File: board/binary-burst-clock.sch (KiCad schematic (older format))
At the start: 24 parts, among them J1 USB, P01 CONN_5, P02 CONN_5, P03 CONN_5, P04 CONN_5, P05 CONN_5, P06 CONN_5, P07 CONN_5, P08 CONN_5, P09 CONN_5, P10 CONN_5, P11 CONN_5, P12 CONN_5, Q1 2907A, Q2 2907A, Q3 2907A, Q4 2907A, U1 ATTINY44, U2 MCP7940N, U3 STP16CP05MTR

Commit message: More schematic work
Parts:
- added CONN1: K3000, symbol K3000
- added J2: AVR-ISP-6, AVR-ISP-6, symbol AVR-ISP-6
- added R?: R, symbol R
- added SW1, SW2: SW_PUSH, symbol SW_PUSH
- added X1: 32.768 kHz CRYSTAL, symbol CRYSTAL
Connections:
- net labels added: +BATT, PA5, Reset, SCL, SDA
- wire segments 102 -> 136
- no-connect marks 6 -> 7
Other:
- note added: "CR1220 Backup Battery"
- moved on the sheet: P01, P02, P03, P04, P05, P06, P07, P08, P09, P10, P11, P12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

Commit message: Full schematic finished
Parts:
- added R? (x4): 1k, symbol R
- added R? (x3): 2056, symbol R
- R?: value R -> 10k
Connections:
- net labels added: Blue0, Blue1, Blue2, Clock, Data, Latch, PA7, Red0
- wire segments 136 -> 169
- no-connect marks 7 -> 8
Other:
- moved on the sheet: P01, P02, P03, P04, P05, P06, P07, P12, R?, SW1, SW2, U1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

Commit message: All footprints created and assigned
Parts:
- removed J2: AVR-ISP-6, AVR-ISP-6, symbol AVR-ISP-6
- added CON1: AVR-ISP-6-FIXED, AVR_ISP_6-fixed, symbol AVR-ISP-6-FIXED
- P1: renamed from P01; value CONN_5 -> 1:00
- P10: value CONN_5 -> 10:00
- P11: value CONN_5 -> 11:00
- P12: value CONN_5 -> 12:00
- P2: renamed from P02; value CONN_5 -> 2:00
- P3: renamed from P03; value CONN_5 -> 3:00
- P4: renamed from P04; value CONN_5 -> 4:00
- P5: renamed from P05; value CONN_5 -> 5:00
- P6: renamed from P06; value CONN_5 -> 6:00
- P7: renamed from P07; value CONN_5 -> 7:00
- P8: renamed from P08; value CONN_5 -> 8:00
- P9: renamed from P09; value CONN_5 -> 9:00
- gave numbers to parts that had none: 8
- renumbered R3 to R4
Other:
- moved on the sheet: C3

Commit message: Finished first version of PCB
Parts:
- SW1: value SW_PUSH -> Hours
- SW2: value SW_PUSH -> Minutes
- X1: value 32.768 kHz CRYSTAL -> 32.768
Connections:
- wire segments 169 -> 167
- no-connect marks 8 -> 9

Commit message: Added I2C and power header; adjusted spacing
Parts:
- added P13: I2C, symbol CONN_4
- added P14: Power, symbol CONN_2
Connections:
- wire segments 167 -> 177

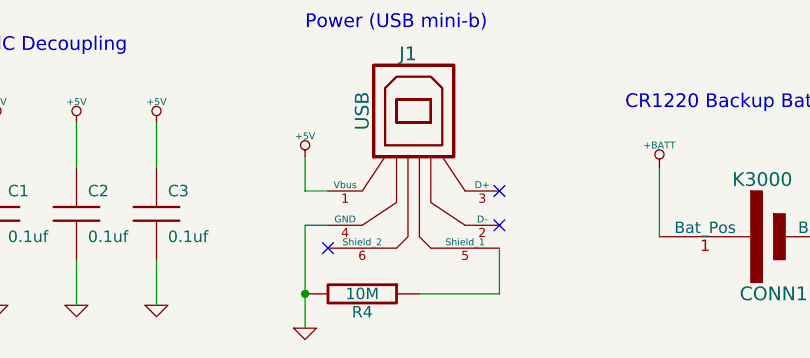
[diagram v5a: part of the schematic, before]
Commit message: Widened all traces (rerouting as neccessary) and removed 10M resistor from USB shielding pin.
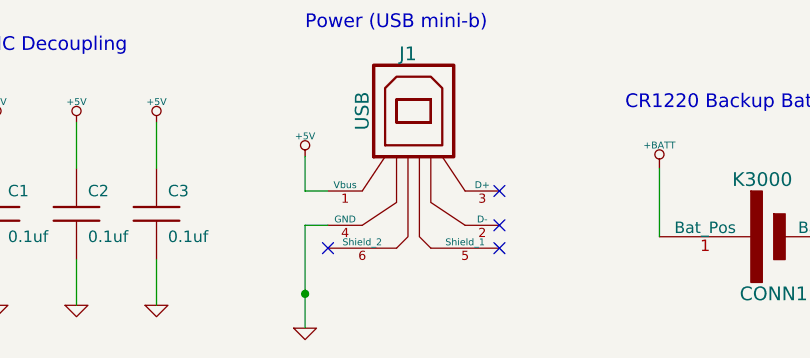
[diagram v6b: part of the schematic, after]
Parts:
- removed R4: 10M, symbol R
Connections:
- wire segments 177 -> 175
- no-connect marks 9 -> 10
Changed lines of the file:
@@
-EESchema Schematic File Version 2  date Mon 26 Dec 2011 10:55:31 AM CST
+EESchema Schematic File Version 2  date Sat 31 Dec 2011 04:27:24 PM CST
 LIBS:power
 LIBS:k3000
@@
 Sheet 1 1
 Title ""
-Date "26 dec 2011"
+Date "31 dec 2011"
 Rev ""
 Comp ""
@@
 Comment4 ""
 $EndDescr
+NoConn ~ 3400 7000
 Wire Wire Line
 	1100 5350 1100 5150
@@
 Wire Wire Line
 	5600 1700 5850 1700
-Wire Wire Line
-	3050 7200 3400 7200
-Wire Wire Line
-	3400 7200 3400 7000
 Wire Wire Line
 	6250 3950 5800 3950
@@
 $EndComp
 $Comp
-L R R4
-U 1 1 4EEDEFC3
-P 2800 7200
-F 0 "R4" V 2880 7200 50  0000 C CNN
-F 1 "10M" V 2800 7200 50  0000 C CNN
-	1    2800 7200
-	0    1    1    0
-$EndComp
-$Comp

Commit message: Fixed USB connector pinout; Adjusted solder stop of SOIC packages; moved labels on silk screen
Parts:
- removed J1: USB, symbol USB
- added J1: MINI_USB-B, symbol MINI_USB-B
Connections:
- no-connect marks 10 -> 9
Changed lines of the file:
@@
-EESchema Schematic File Version 2  date Sat 31 Dec 2011 04:27:24 PM CST
+EESchema Schematic File Version 2  date Sun 01 Jan 2012 04:04:24 PM CST
 LIBS:power
 LIBS:k3000
@@
 LIBS:valves
 LIBS:avr-isp-6
+LIBS:mini_usb-b
 LIBS:binary-burst-clock-cache
 EELAYER 25  0
@@
 Sheet 1 1
 Title ""
-Date "31 dec 2011"
+Date "1 jan 2012"
 Rev ""
 Comp ""
@@
 Comment4 ""
 $EndDescr
-NoConn ~ 3400 7000
+Wire Wire Line
+	2450 6700 2450 6800
+Wire Wire Line
+	2450 6800 2750 6800
 Wire Wire Line
 	1100 5350 1100 5150
@@
 Wire Wire Line
 	2950 5500 2700 5500
-Connection ~ 2550 7200
-Wire Wire Line
-	2650 6900 2550 6900
-Wire Wire Line
-	2550 6900 2550 7350
-Wire Wire Line
-	2650 6750 2550 6750
-Wire Wire Line
-	2550 6750 2550 6600
 Wire Wire Line
 	1900 7050 1900 7250
@@
 Wire Wire Line
 	1100 4950 1100 4750
+Wire Wire Line
+	3250 6800 3450 6800
+Wire Wire Line
+	3450 6800 3450 7000
+NoConn ~ 3150 7100
+NoConn ~ 3000 7100
+NoConn ~ 2850 7100
+$Comp
+L MINI_USB-B J1
+U 1 1 4F00D813
+P 3000 6800
+F 0 "J1" H 2700 6950 60  0000 C CNN
+F 1 "MINI_USB-B" H 3000 7050 60  0000 C CNN
+	1    3000 6800
+	1    0    0    -1
+$EndComp
 $Comp
 L GND #PWR01
@@
 	1    0    0    -1
 $EndComp
-NoConn ~ 2650 7000
 $Comp
 L K3000 CONN1
@@
 	1    0    0    -1
 $EndComp
-Text Notes 2550 6050 0    60   ~ 0
+Text Notes 2550 6400 0    60   ~ 0
 Power (USB mini-b)
-NoConn ~ 3400 6900
-NoConn ~ 3400 6750
 $Comp
 L +5V #PWR017
 U 1 1 4EEDF02B
-P 2550 6600
-F 0 "#PWR017" H 2550 6690 20  0001 C CNN
-F 1 "+5V" H 2550 6690 30  0000 C CNN
-	1    2550 6600
+P 2450 6700
+F 0 "#PWR017" H 2450 6790 20  0001 C CNN
+F 1 "+5V" H 2450 6790 30  0000 C CNN
+	1    2450 6700
 	1    0    0    -1
 $EndComp
@@
 L GND #PWR018
 U 1 1 4EEDF025
-P 2550 7350
-F 0 "#PWR018" H 2550 7350 30  0001 C CNN
-F 1 "GND" H 2550 7280 30  0001 C CNN
-	1    2550 7350
-	1    0    0    -1
-$EndComp
-$Comp
-L USB J1
-U 1 1 4EEDEEC4
-P 3050 6550
-F 0 "J1" H 3000 6950 60  0000 C CNN
-F 1 "USB" V 2800 6700 60  0000 C CNN
-	1    3050 6550
-	1    0    0    -1
-$EndComp
+P 3450 7000
+F 0 "#PWR018" H 3450 7000 30  0001 C CNN
+F 1 "GND" H 3450 6930 30  0001 C CNN
+	1    3450 7000
+	1    0    0    -1
+$EndComp

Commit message: Added status LED; cleaned up GND traces
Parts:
- added D1: LED, symbol LED
- added R4: 220, symbol R
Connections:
- wire segments 175 -> 178
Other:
- note added: "Status LED"
